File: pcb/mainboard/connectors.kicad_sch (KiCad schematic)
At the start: 48 parts, among them J28 SMPM, J29 SMPM, J30 SMPM, J31 SMPM, J32 SMPM, J33 SMPM, J34 SMPM, J35 SMPM, J36 SMPM, J37 SMPM, J38 SMPM, J39 SMPM, J40 SMPM, J41 SMPM, J42 SMPM, J43 SMPM, J44 SMPM, J45 SMPM, J46 SMPM, J47 SMPM, K1 RELAY_TE_HF3_96, K2 RELAY_TE_HF3_96, K3 RELAY_TE_HF3_96, K4 RELAY_TE_HF3_96, U55 BD63573NUV, U56 BD63573NUV, U57 BD63573NUV, U58 BD63573NUV

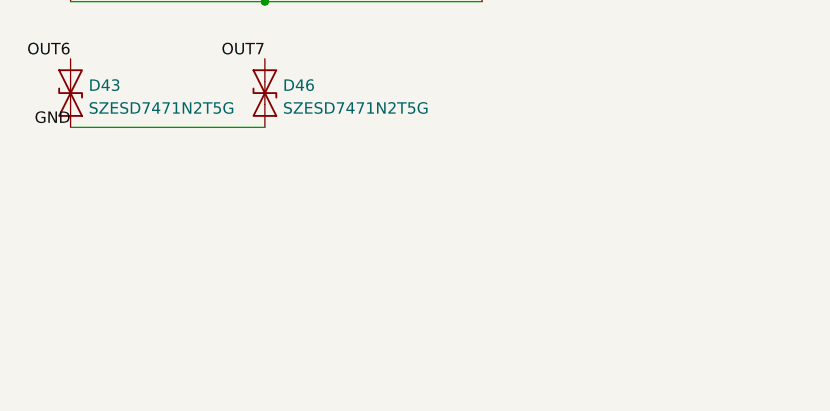
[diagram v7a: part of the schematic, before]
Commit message: Initial FPGA routing
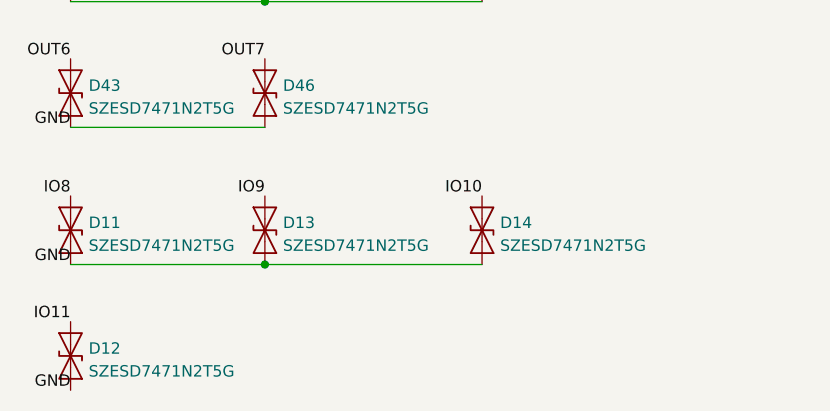
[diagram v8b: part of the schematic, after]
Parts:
- added D11, D12, D13, D14: SZESD7471N2T5G, azonenberg_pcb:SOD882, symbol device:D_TVS
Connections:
- net GND: now also D11.1 (A1), D12.1 (A1), D13.1 (A1), D14.1 (A1)
- net IO10: now also D14.2 (A2)
- net IO11: now also D12.2 (A2)
- net IO8: now also D11.2 (A2)
- net IO9: now also D13.2 (A2)
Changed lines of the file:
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@@
   (title_block
     (title "Trigger Crossbar")
-    (date "2023-12-20")
+    (date "2023-12-22")
     (rev "0.1")
     (company "Antikernel Labs")
@@
   (junction (at 179.07 60.96) (diameter 0) (color 0 0 0 0)
   )
+  (junction (at 43.18 158.75) (diameter 0) (color 0 0 0 0)
+  )
   (junction (at 179.07 58.42) (diameter 0) (color 0 0 0 0)
   )
@@
     (stroke (width 0) (type default) (color 0 0 0 0))
   )
+  (wire (pts (xy 21.59 158.75) (xy 43.18 158.75))
+    (stroke (width 0) (type default) (color 0 0 0 0))
+  )
   (wire (pts (xy 142.24 60.96) (xy 142.24 63.5))
     (stroke (width 0) (type default) (color 0 0 0 0))
@@
     (stroke (width 0) (type default) (color 0 0 0 0))
   )
+  (wire (pts (xy 43.18 158.75) (xy 67.31 158.75))
+    (stroke (width 0) (type default) (color 0 0 0 0))
+  )
   (wire (pts (xy 142.24 25.4) (xy 142.24 27.94))
     (stroke (width 0) (type default) (color 0 0 0 0))
@@
     (effects (font (size 1.27 1.27)) (justify left bottom))
   )
+  (label "GND" (at 21.59 158.75 180)
+    (effects (font (size 1.27 1.27)) (justify right bottom))
+  )
   (label "GND" (at 63.5 99.06 0)
     (effects (font (size 1.27 1.27)) (justify left bottom))
@@
     (effects (font (size 1.27 1.27)) (justify right bottom))
   )
+  (label "IO8" (at 21.59 151.13 180)
+    (effects (font (size 1.27 1.27)) (justify right bottom))
+  )
   (label "GND" (at 21.59 143.51 180)
     (effects (font (size 1.27 1.27)) (justify right bottom))
@@
     (effects (font (size 1.27 1.27)) (justify right bottom))
   )
+  (label "IO11" (at 21.59 165.1 180)
+    (effects (font (size 1.27 1.27)) (justify right bottom))
+  )
   (label "GND" (at 39.37 68.58 0)
     (effects (font (size 1.27 1.27)) (justify left bottom))
@@
     (effects (font (size 1.27 1.27)) (justify right bottom))
   )
+  (label "IO9" (at 43.18 151.13 180)
+    (effects (font (size 1.27 1.27)) (justify right bottom))
+  )
   (label "CH8_COIL_N" (at 116.84 40.64 180)
     (effects (font (size 1.27 1.27)) (justify right bottom))
@@
     (effects (font (size 1.27 1.27)) (justify left bottom))
   )
+  (label "GND" (at 21.59 172.72 180)
+    (effects (font (size 1.27 1.27)) (justify right bottom))
+  )
   (label "12V0" (at 179.07 93.98 180)
     (effects (font (size 1.27 1.27)) (justify right bottom))
@@
   (label "CH8_COIL_N" (at 142.24 40.64 0)
     (effects (font (size 1.27 1.27)) (justify left bottom))
+  )
+  (label "IO10" (at 67.31 151.13 180)
+    (effects (font (size 1.27 1.27)) (justify right bottom))
   )
   (label "3V3" (at 179.07 91.44 180)
@@
     (pin "2")
   )
+  (symbol (lib_id "device:D_TVS") (at 67.31 154.94 90) (unit 1)
+    (in_bom yes) (on_board yes) (fields_autoplaced)
+    (property "Reference" "D14" (id 0) (at 69.3166 154.1053 90)
+      (effects (font (size 1.27 1.27)) (justify right))
+    )
+    (property "Value" "SZESD7471N2T5G" (id 1) (at 69.3166 156.6422 90)
+      (effects (font (size 1.27 1.27)) (justify right))
+    )
+    (property "Footprint" "azonenberg_pcb:SOD882" (id 2) (at 67.31 154.94 0)
+      (effects (font (size 1.27 1.27)) hide)
+    )
+    (property "Datasheet" "https://en.wikipedia.org/wiki/Transient-voltage-suppression_diode" (id 3) (at 67.31 154.94 0)
+      (effects (font (size 1.27 1.27)) hide)
+    )
+    (pin "1")
+    (pin "2")
+  )
   (symbol (lib_id "conn:CONN_COAXIAL") (at 21.59 21.59 0) (mirror y) (unit 1)
     (in_bom yes) (on_board yes) (fields_autoplaced)
@@
     (pin "8")
     (pin "9")
+  )
+  (symbol (lib_id "device:D_TVS") (at 43.18 154.94 90) (unit 1)
+    (in_bom yes) (on_board yes) (fields_autoplaced)
+    (property "Reference" "D13" (id 0) (at 45.1866 154.1053 90)
+      (effects (font (size 1.27 1.27)) (justify right))
+    )
+    (property "Value" "SZESD7471N2T5G" (id 1) (at 45.1866 156.6422 90)
+      (effects (font (size 1.27 1.27)) (justify right))
+    )
+    (property "Footprint" "azonenberg_pcb:SOD882" (id 2) (at 43.18 154.94 0)
+      (effects (font (size 1.27 1.27)) hide)
+    )
+    (property "Datasheet" "https://en.wikipedia.org/wiki/Transient-voltage-suppression_diode" (id 3) (at 43.18 154.94 0)
+      (effects (font (size 1.27 1.27)) hide)
+    )
+    (pin "1")
+    (pin "2")
   )
   (symbol (lib_id "conn:CONN_COAXIAL") (at 50.8 80.01 0) (mirror y) (unit 1)
@@
     (pin "7")
   )
+  (symbol (lib_id "device:D_TVS") (at 21.59 154.94 90) (unit 1)
+    (in_bom yes) (on_board yes) (fields_autoplaced)
+    (property "Reference" "D11" (id 0) (at 23.5966 154.1053 90)
+      (effects (font (size 1.27 1.27)) (justify right))
+    )
+    (property "Value" "SZESD7471N2T5G" (id 1) (at 23.5966 156.6422 90)
+      (effects (font (size 1.27 1.27)) (justify right))
+    )
+    (property "Footprint" "azonenberg_pcb:SOD882" (id 2) (at 21.59 154.94 0)
+      (effects (font (size 1.27 1.27)) hide)
+    )
+    (property "Datasheet" "https://en.wikipedia.org/wiki/Transient-voltage-suppression_diode" (id 3) (at 21.59 154.94 0)
+      (effects (font (size 1.27 1.27)) hide)
+    )
+    (pin "1")
+    (pin "2")
+  )
   (symbol (lib_id "device:D_TVS") (at 67.31 125.73 90) (unit 1)
     (in_bom yes) (on_board yes) (fields_autoplaced)
@@
       (effects (font (size 1.27 1.27)) hide)
     )
+    (pin "1")
+    (pin "2")
+  )
+  (symbol (lib_id "device:D_TVS") (at 21.59 168.91 90) (unit 1)
+    (in_bom yes) (on_board yes) (fields_autoplaced)
+    (property "Reference" "D12" (id 0) (at 23.5966 168.0753 90)
+      (effects (font (size 1.27 1.27)) (justify right))
+    )
+    (property "Value" "SZESD7471N2T5G" (id 1) (at 23.5966 170.6122 90)
+      (effects (font (size 1.27 1.27)) (justify right))
+    )
+    (property "Footprint" "azonenberg_pcb:SOD882" (id 2) (at 21.59 168.91 0)
+      (effects (font (size 1.27 1.27)) hide)
+    )
+    (property "Datasheet" "https://en.wikipedia.org/wiki/Transient-voltage-suppression_diode" (id 3) (at 21.59 168.91 0)
+      (effects (font (size 1.27 1.27)) hide)
+    )
